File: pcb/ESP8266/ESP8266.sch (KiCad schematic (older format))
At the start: 18 parts, among them J1 Conn_02x04, U1 ESP8266EX, U2 W25Q16BVSSIG

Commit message: mejoras en el pcb
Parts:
- J1: footprint Connector_PinHeader_1.27mm:PinHeader_2x04_P1.27mm_Vertical -> Connector_PinHeader_2.54mm:PinHeader_2x04_P2.54mm_Vertical
- U1: Field4 IPC-7351B -> https://www.digikey.com/es/products/detail/espressif-system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
- U2: Field4 F -> https://www.digikey.com/es/products/detail/winbond-electron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
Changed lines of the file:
@@
 Rev "v1.0"
 Comp "CESE11 - Federico Pacher"
-Comment1 ""
+Comment1 "Revisor Hanes Sciarrone"
 Comment2 ""
 Comment3 ""
@@
 F 2 "W25Q16BVSSIG:SOIC127P790X216-8N" H 3025 3700 50  0001 L BNN
 F 3 "https://media.digikey.com/pdf/Data%20Sheets/Winbond%20PDFs/W25Q64BV.pdf" H 3025 3700 50  0001 L BNN
-F 4 "F" H 3025 3700 50  0001 L BNN "Field4"
+F 4 "https://www.digikey.com/es/products/detail/winbond-electronics/W25Q16BVSSIG/2208449" H 3025 3700 50  0001 L BNN "Field4"
 F 5 "IPC-7351B" H 3025 3700 50  0001 L BNN "Field5"
 	1    3025 3700
@@
 NoConn ~ 6600 3575
 $Comp
-L Device:L L2
-U 1 1 5F63F49C
-P 8600 3225
-F 0 "L2" H 8652 3271 50  0000 L CNN
-F 1 "NC" H 8652 3180 50  0000 L CNN
-F 2 "Inductor_SMD:L_0402_1005Metric" H 8600 3225 50  0001 C CNN
-F 3 "~" H 8600 3225 50  0001 C CNN
-	1    8600 3225
-	-1   0    0    -1
-$EndComp
-$Comp
-L Device:L L1
-U 1 1 5F6400FC
-P 9200 3225
-F 0 "L1" H 9250 3175 50  0000 L CNN
-F 1 "NC" H 9250 3250 50  0000 L CNN
-F 2 "Inductor_SMD:L_0402_1005Metric" H 9200 3225 50  0001 C CNN
-F 3 "~" H 9200 3225 50  0001 C CNN
-	1    9200 3225
-	1    0    0    1
-$EndComp
-$Comp
 L power:GND #PWR0112
 U 1 1 5F6405DA
@@
 	-1   0    0    -1
 $EndComp
-Wire Wire Line
-	8750 3075 8600 3075
-Connection ~ 8600 3075
 Wire Wire Line
 	9050 3075 9200 3075
@@
 F 0 "J1" H 9650 2217 50  0000 C CNN
 F 1 "Conn_02x04" H 9650 2126 50  0000 C CNN
-F 2 "Connector_PinHeader_1.27mm:PinHeader_2x04_P1.27mm_Vertical" H 9600 1900 50  0001 C CNN
+F 2 "Connector_PinHeader_2.54mm:PinHeader_2x04_P2.54mm_Vertical" H 9600 1900 50  0001 C CNN
 F 3 "~" H 9600 1900 50  0001 C CNN
 	1    9600 1900
@@
 Capacitores de desacople
 Wire Wire Line
-	6600 3075 8600 3075
-Wire Wire Line
 	3325 2625 3325 2700
 Wire Wire Line
@@
 Wire Wire Line
 	7350 2475 7350 2550
-Wire Wire Line
-	9200 3375 9200 3450
-Wire Wire Line
-	8600 3375 8600 3450
 Wire Wire Line
 	9950 2000 9950 2225
@@
 F 2 "ESP8266EX:QFN50P500X500X80-33N" H 5700 3075 50  0001 L BNN
 F 3 "https://www.espressif.com/sites/default/files/documentation/0a-esp8266ex_datasheet_en.pdf" H 5700 3075 50  0001 L BNN
-F 4 "IPC-7351B" H 5700 3075 50  0001 L BNN "Field4"
+F 4 "https://www.digikey.com/es/products/detail/espressif-systems/ESP8266EX/8028408?utm_adgroup=RF%20%26%20RFID&utm_source=google&utm_medium=cpc&utm_campaign=ES_Argentina_Dynamic%20Search&utm_term=&utm_content=RF%20%26%20RFID&gclid=CjwKCAjwlID8BRAFEiwAnUoK1Yae-m8mh8PoYFFlH1WCcLQath7XOvYnJY-aIz6l4-U5oYpn0OpbJBoC5OwQAvD_BwE" H 5700 3075 50  0001 L BNN "Field4"
 F 5 "36610" H 5700 3075 50  0001 L BNN "Field5"
 F 6 "Espressif Systems" H 5700 3075 50  0001 L BNN "Field6"
@@
 Wire Wire Line
 	1600 4550 6675 4550
+$Comp
+L Device:L L1
+U 1 1 5F6400FC
+P 9200 3225
+F 0 "L1" H 9250 3175 50  0000 L CNN
+F 1 "NC" H 9250 3250 50  0000 L CNN
+F 2 "Inductor_SMD:L_0402_1005Metric" H 9200 3225 50  0001 C CNN
+F 3 "~" H 9200 3225 50  0001 C CNN
+	1    9200 3225
+	1    0    0    1
+$EndComp
+Wire Wire Line
+	9200 3375 9200 3450
+$Comp
+L Device:L L2
+U 1 1 5F63F49C
+P 8600 3225
+F 0 "L2" H 8652 3271 50  0000 L CNN
+F 1 "NC" H 8652 3180 50  0000 L CNN
+F 2 "Inductor_SMD:L_0402_1005Metric" H 8600 3225 50  0001 C CNN
+F 3 "~" H 8600 3225 50  0001 C CNN
+	1    8600 3225
+	-1   0    0    -1
+$EndComp
+Wire Wire Line
+	8600 3375 8600 3450
+Wire Wire Line
+	6600 3075 8600 3075
+Wire Wire Line
+	8750 3075 8600 3075
+Connection ~ 8600 3075
 $EndSCHEMATC

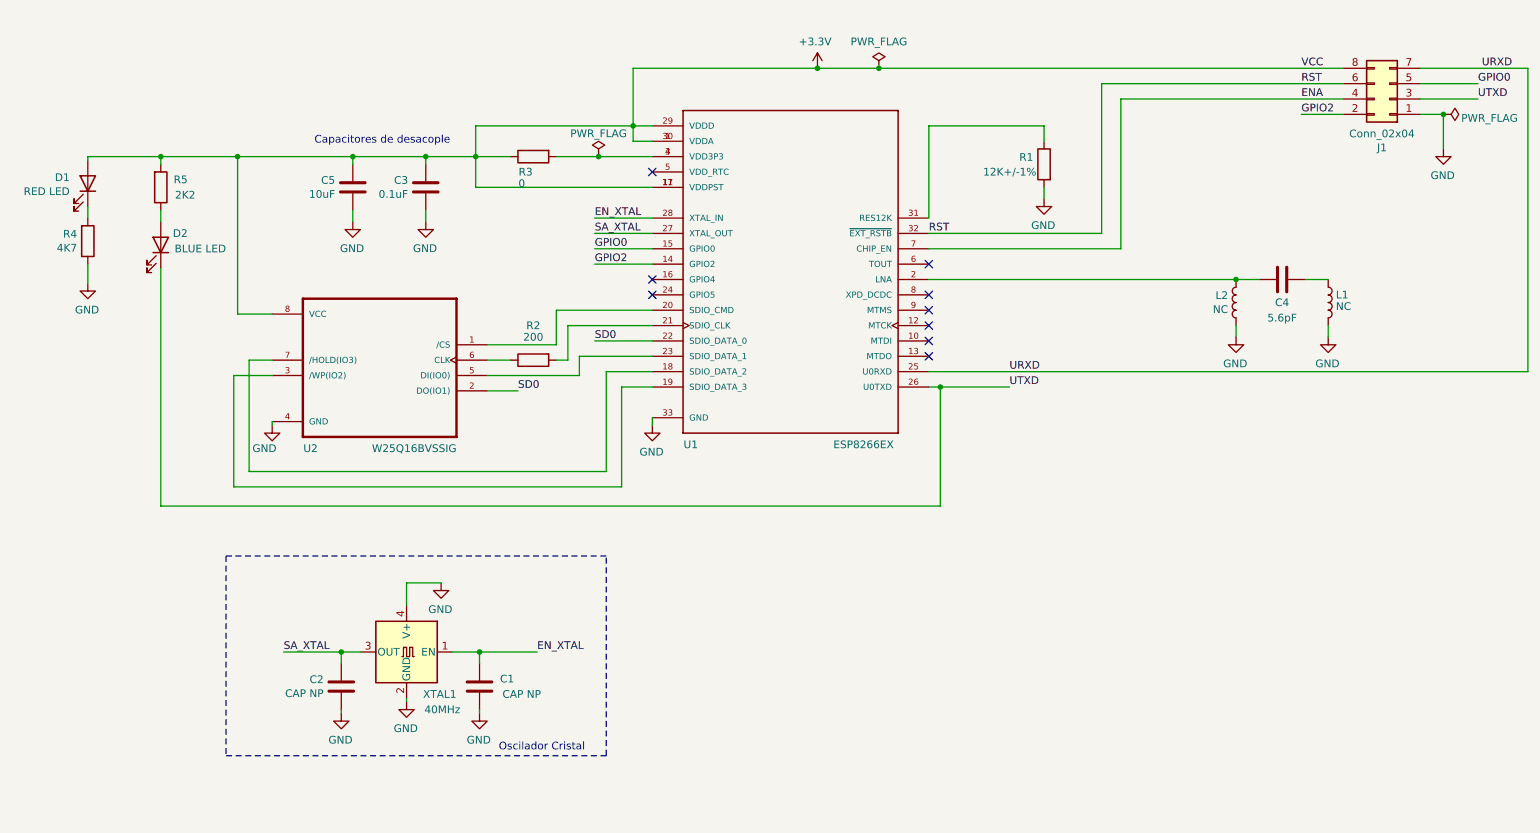
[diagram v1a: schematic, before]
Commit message: agregado de modelos 3D al proeycto, fiduciales y agujero
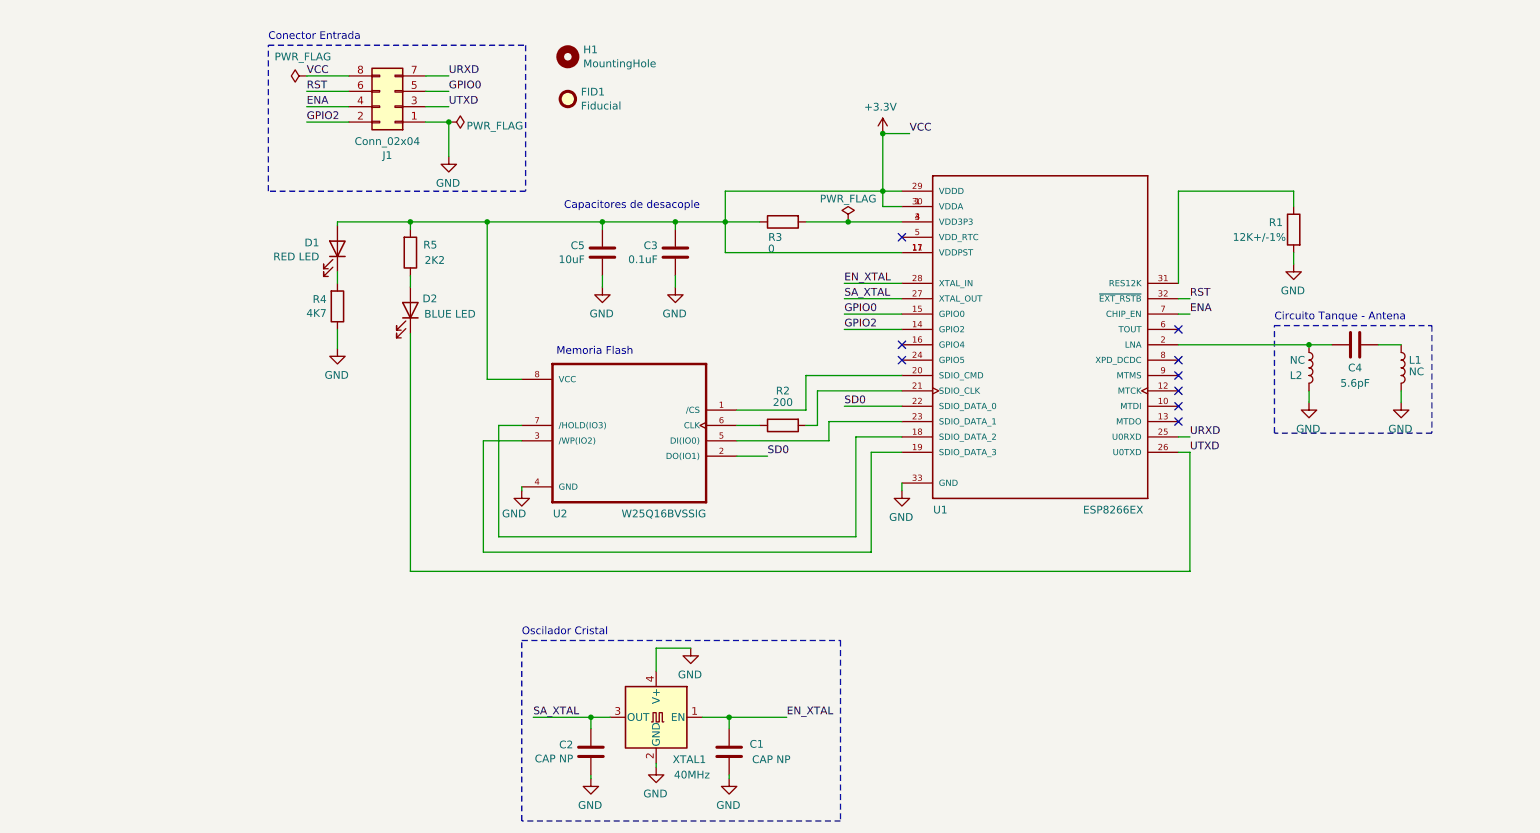
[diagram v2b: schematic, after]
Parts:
- added FID1: Fiducial, Fiducial:Fiducial_0.5mm_Mask1mm, symbol Mechanical:Fiducial
- added H1: MountingHole, MountingHole:MountingHole_2mm, symbol Mechanical:MountingHole
- XTAL1: Field4 (none) -> https://www.digikey.com/en/products/detail/abracon-llc/ABM8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
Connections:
- net GND: now also L2.1; no longer L2.2
- net at C4.1, U1.2 (LNA): now also L2.2; no longer L2.1
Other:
- note added: "Circuito Tanque - Antena"
- note added: "Conector Entrada"
- note added: "Memoria Flash"
- moved on the sheet: C1, C2, C3, C4, C5, D1, D2, J1, L1, L2, R1, R2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

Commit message: correcciones
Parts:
- added FID2, FID3: Fiducial, Fiducial:Fiducial_1mm_Mask2mm, symbol Mechanical:Fiducial
- FID1: footprint Fiducial:Fiducial_0.5mm_Mask1mm -> Fiducial:Fiducial_1mm_Mask2mm
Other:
- note added: "Agujero sugeción"
- note added: "Fiduciales"
- moved on the sheet: FID1, H1
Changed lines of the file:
@@
 L Mechanical:MountingHole H1
 U 1 1 5F8A9382
-P 4250 1625
-F 0 "H1" H 4350 1671 50  0000 L CNN
-F 1 "MountingHole" H 4350 1580 50  0000 L CNN
-F 2 "MountingHole:MountingHole_2mm" H 4250 1625 50  0001 C CNN
-F 3 "~" H 4250 1625 50  0001 C CNN
-	1    4250 1625
+P 1050 1625
+F 0 "H1" H 1150 1671 50  0000 L CNN
+F 1 "MountingHole" H 1150 1580 50  0000 L CNN
+F 2 "MountingHole:MountingHole_2mm" H 1050 1625 50  0001 C CNN
+F 3 "~" H 1050 1625 50  0001 C CNN
+	1    1050 1625
 	1    0    0    -1
 $EndComp
@@
 L Mechanical:Fiducial FID1
 U 1 1 5F8B2921
-P 4250 1900
-F 0 "FID1" H 4335 1946 50  0000 L CNN
-F 1 "Fiducial" H 4335 1855 50  0000 L CNN
-F 2 "Fiducial:Fiducial_0.5mm_Mask1mm" H 4250 1900 50  0001 C CNN
-F 3 "~" H 4250 1900 50  0001 C CNN
-	1    4250 1900
+P 1025 2250
+F 0 "FID1" H 1110 2296 50  0000 L CNN
+F 1 "Fiducial" H 1110 2205 50  0000 L CNN
+F 2 "Fiducial:Fiducial_1mm_Mask2mm" H 1025 2250 50  0001 C CNN
+F 3 "~" H 1025 2250 50  0001 C CNN
+	1    1025 2250
 	1    0    0    -1
 $EndComp
+$Comp
+L Mechanical:Fiducial FID2
+U 1 1 5F8B46CF
+P 1025 2475
+F 0 "FID2" H 1110 2521 50  0000 L CNN
+F 1 "Fiducial" H 1110 2430 50  0000 L CNN
+F 2 "Fiducial:Fiducial_1mm_Mask2mm" H 1025 2475 50  0001 C CNN
+F 3 "~" H 1025 2475 50  0001 C CNN
+	1    1025 2475
+	1    0    0    -1
+$EndComp
+$Comp
+L Mechanical:Fiducial FID3
+U 1 1 5F8B4929
+P 1025 2725
+F 0 "FID3" H 1110 2771 50  0000 L CNN
+F 1 "Fiducial" H 1110 2680 50  0000 L CNN
+F 2 "Fiducial:Fiducial_1mm_Mask2mm" H 1025 2725 50  0001 C CNN
+F 3 "~" H 1025 2725 50  0001 C CNN
+	1    1025 2725
+	1    0    0    -1
+$EndComp
+Wire Notes Line
+	850  2075 1525 2075
+Wire Notes Line
+	1525 2075 1525 2900
+Wire Notes Line
+	1525 2900 850  2900
+Wire Notes Line
+	850  2900 850  2075
+Wire Notes Line
+	850  1450 850  1800
+Wire Notes Line
+	850  1800 1750 1800
+Wire Notes Line
+	1750 1800 1750 1450
+Wire Notes Line
+	1750 1450 850  1450
+Text Notes 850  1425 0    50   ~ 0
+Agujero sugeción
+Text Notes 850  2050 0    50   ~ 0
+Fiduciales
 $EndSCHEMATC

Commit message: reacomodamiento en esquematico
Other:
- note added: "Agujero sujeción"
- note removed: "Agujero sugeción"
